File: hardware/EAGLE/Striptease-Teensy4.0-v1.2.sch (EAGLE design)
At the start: 18 parts, among them IC1 74245N

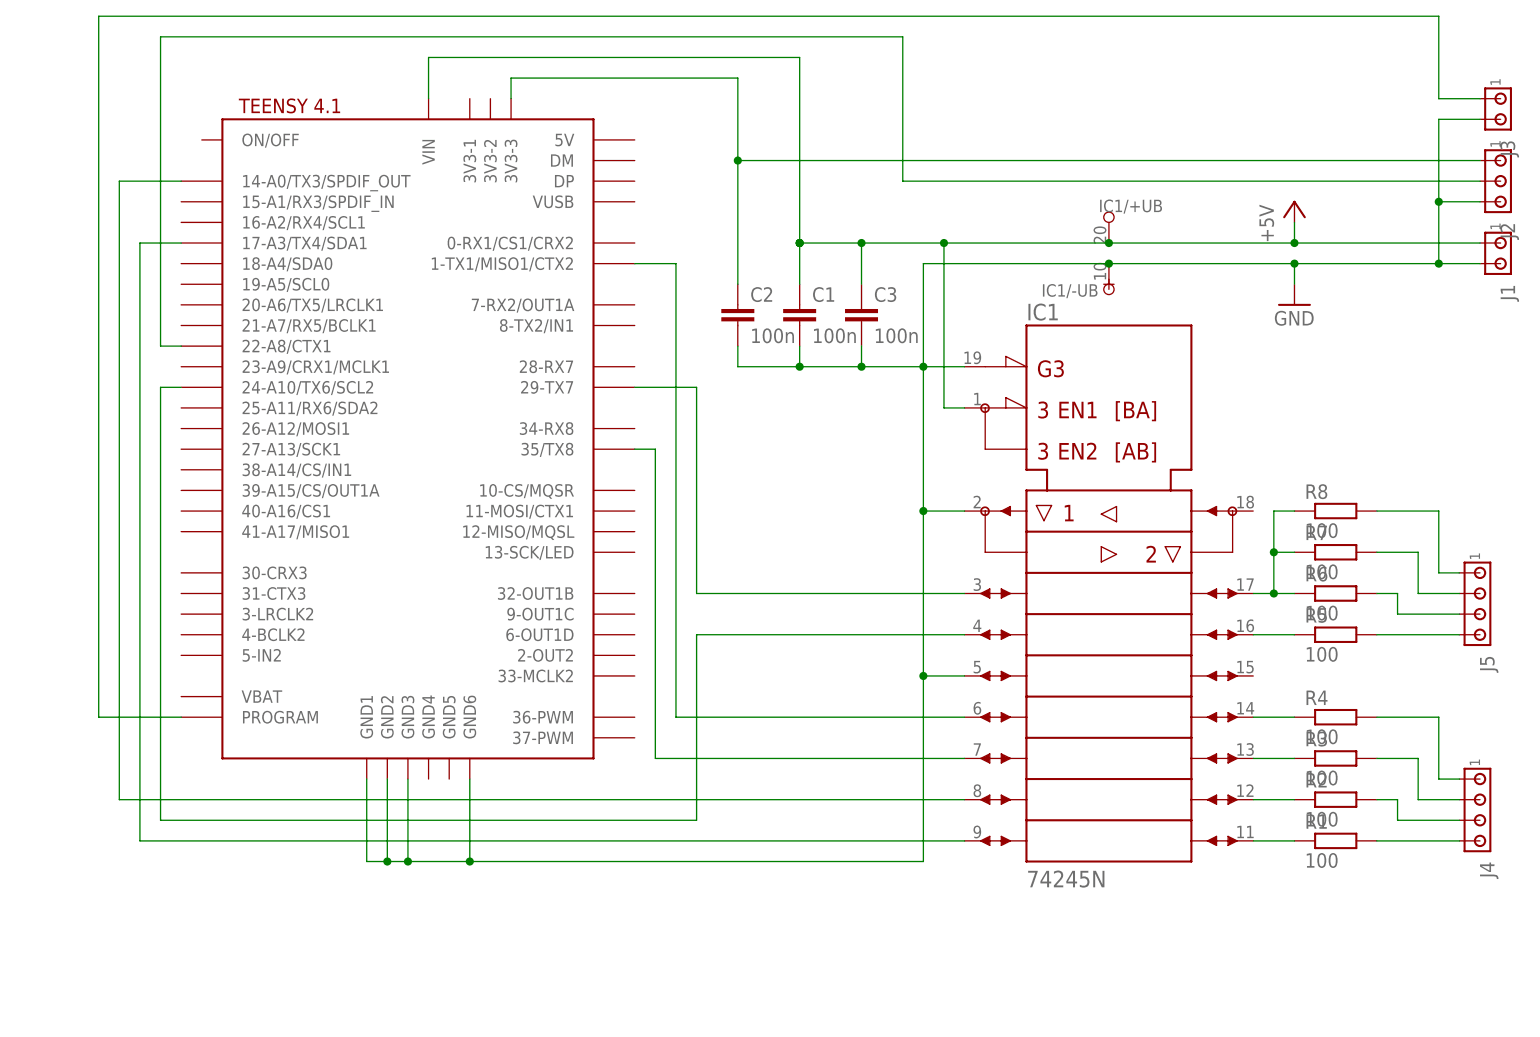
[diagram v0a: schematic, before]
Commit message: Change connector names in EAGLE boards.
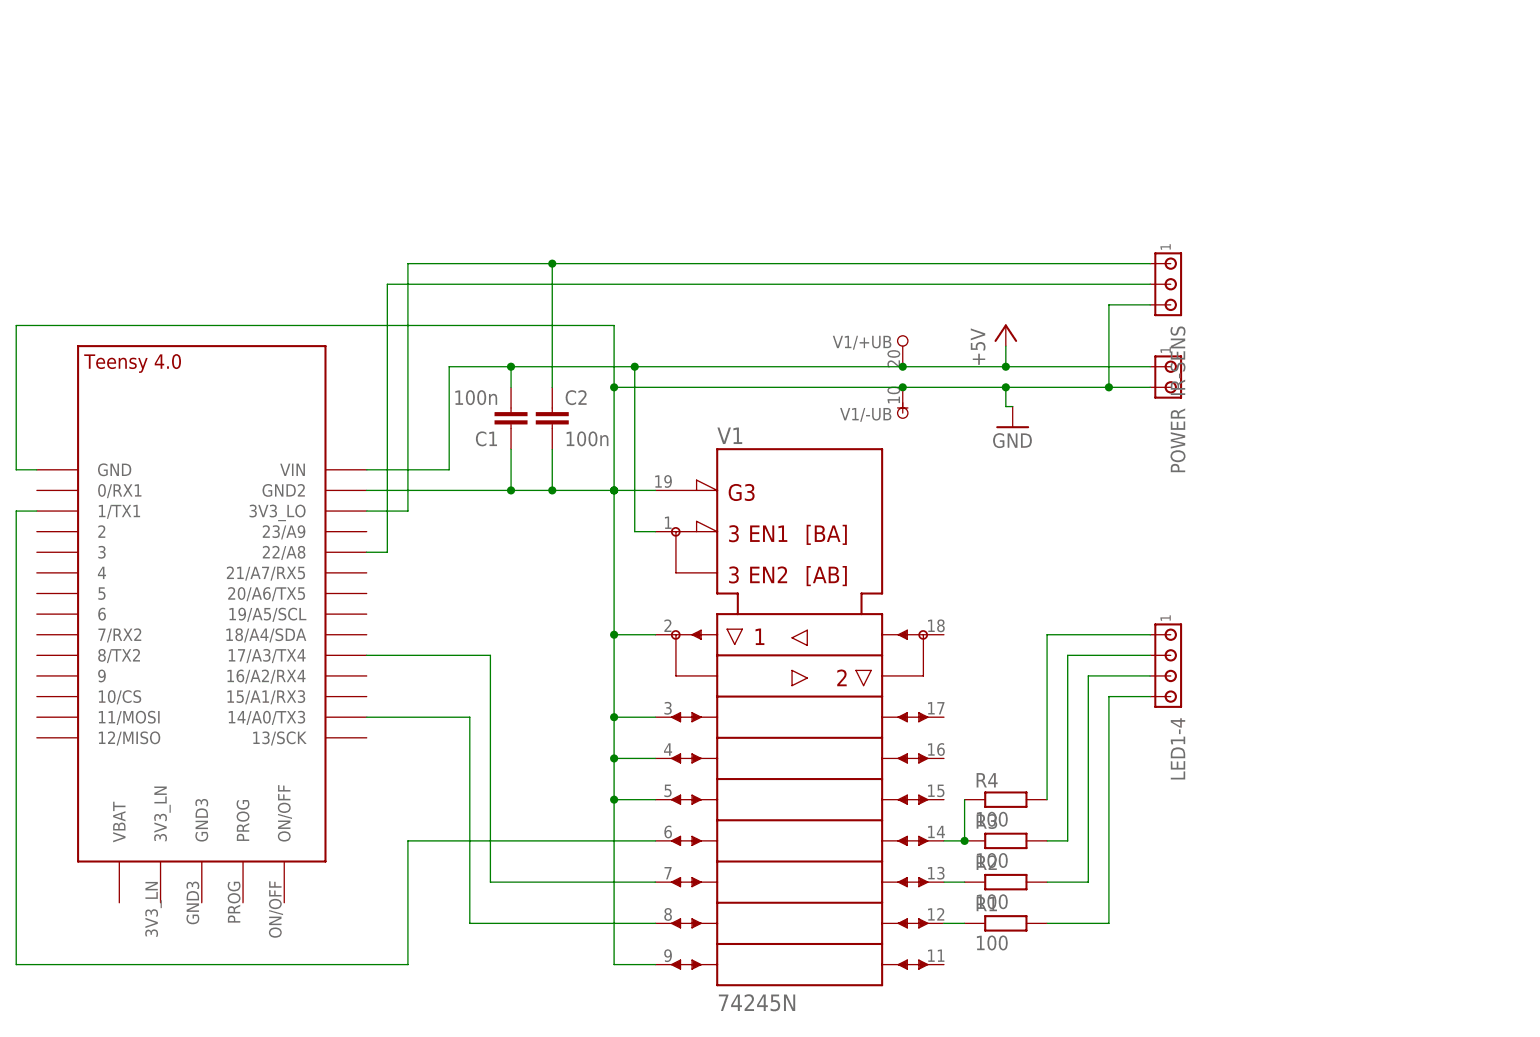
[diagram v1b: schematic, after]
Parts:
- removed C3: 100n, rcl:C-EU050-025X075
- removed IC1: 74245N, 74ttl-din:74245N
- removed J1, J3: (no value), con-amp:MTA02-100
- removed J2: (no value), con-amp:MTA03-100
- removed J4, J5: (no value), con-amp:MTA04-100
- removed R5, R6, R7, R8: 100, rcl:R-EU_0207/10
- removed U$3: TEENSY41-E, teensy:TEENSY41-E
- added IR-SENS: (no value), con-amp:MTA03-100
- added LED1-4: (no value), con-amp:MTA04-100
- added POWER: (no value), con-amp:MTA02-100
- added U$1: TEENSY_4.0-BASIC, Teensy-4.0:TEENSY_4.0-BASIC
- added V1: 74245N, 74ttl-din:74245N
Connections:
- removed net N$16: IC11.B5, R4.1
- removed net N$19: J4.1, R4.2
- removed net N$20: J5.4, R5.2
- removed net N$22: J5.3, R6.2
- removed net N$23: IC11.A8, U$3.17-A3/TX4/SDA1
- removed net N$24: IC11.A7, U$3.14-A0/TX3/SPDIF_OUT
- removed net N$25: IC11.A6, U$3.35/TX8
- removed net N$26: IC11.A5, U$3.1-TX1/MISO1/CTX2
- removed net N$27: IC11.A3, U$3.24-A10/TX6/SCL2
- removed net N$28: IC11.A2, U$3.29-TX7
- removed net N$3: IC11.B3, R5.1
- removed net N$31: J2.2, U$3.22-A8/CTX1
- removed net N$6: J5.2, R7.2
- new net N$21: U$1.1/TX1, V11.A5
- new net N$5: LED1-4.1, R4.2
- net +5V: now also C1.2, POWER.1, U$1.VIN, V1/+UB.+UB, V11.DIR; no longer C1.1, C3.1, IC1/+UB.+UB, IC11.DIR, J1.1, U$3.VIN
- net GND: now also C1.1, IR-SENS.3, POWER.2, U$1.GND, U$1.GND2, V1/-UB.-UB, V11.!G, V11.A1, V11.A2, V11.A3, V11.A4, V11.A8; no longer C1.2, C3.2, IC1/-UB.-UB, IC11.!G, IC11.A1, IC11.A4, J1.2, J2.3, J3.2, U$3.GND1, U$3.GND2, U$3.GND3, U$3.GND6
- net N$1: now also IR-SENS.2, U$1.22/A8; no longer C2.1, J2.1, U$3.3V3-3
- net N$10: now also U$1.14/A0/TX3, V11.A7; no longer J5.1, R8.2
- net N$11: now also V11.B7; no longer IC11.B8
- net N$12: now also V11.B6; no longer IC11.B7
- net N$13: now also R4.1, V11.B5; no longer IC11.B6
- net N$14: now also U$1.17/A3/TX4, V11.A6; no longer IC11.B2, R6.1, R7.1, R8.1
- net N$2: now also C2.1, IR-SENS.1, U$1.3V3_LO; no longer J3.1, U$3.PROGRAM
- net N$7: now also LED1-4.2; no longer J4.2
- net N$8: now also LED1-4.3; no longer J4.3
- net N$9: now also LED1-4.4; no longer J4.4
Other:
- moved on the sheet: C1, C2, R1, R2, R3, R4

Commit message: Add connector pinout for LEDs in EAGLE boards.
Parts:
- renumbered IR-SENS to IR-RECV
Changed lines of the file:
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@@
 <part name="R3" library="rcl" library_urn="urn:adsk.eagle:library:334" deviceset="R-EU_" device="0207/10" package3d_urn="urn:adsk.eagle:package:23491/2" value="100"/>
 <part name="LED1-4" library="con-amp" library_urn="urn:adsk.eagle:library:127" deviceset="MTA04-100" device="" package3d_urn="urn:adsk.eagle:package:8081620/1"/>
-<part name="IR-SENS" library="con-amp" library_urn="urn:adsk.eagle:library:127" deviceset="MTA03-100" device="" package3d_urn="urn:adsk.eagle:package:8081621/1"/>
+<part name="IR-RECV" library="con-amp" library_urn="urn:adsk.eagle:library:127" deviceset="MTA03-100" device="" package3d_urn="urn:adsk.eagle:package:8081621/1"/>
 <part name="POWER" library="con-amp" library_urn="urn:adsk.eagle:library:127" deviceset="MTA02-100" device="" package3d_urn="urn:adsk.eagle:package:8081649/1"/>
 <part name="P+1" library="supply1" library_urn="urn:adsk.eagle:library:371" deviceset="+5V" device=""/>
@@
 <attribute name="VALUE" x="143.51" y="35.56" size="1.778" layer="96" rot="R270"/>
 </instance>
-<instance part="IR-SENS" gate="G$1" x="147.32" y="88.9" smashed="yes" rot="R270">
+<instance part="IR-RECV" gate="G$1" x="147.32" y="88.9" smashed="yes" rot="R270">
 <attribute name="NAME" x="147.32" y="83.82" size="1.778" layer="95" rot="R270"/>
 <attribute name="VALUE" x="143.51" y="83.82" size="1.778" layer="96" rot="R270"/>
@@
 <pinref part="U$1" gate="G$1" pin="22/A8"/>
 <wire x1="50.8" y1="55.88" x2="48.26" y2="55.88" width="0.1524" layer="91"/>
-<pinref part="IR-SENS" gate="G$1" pin="2"/>
+<pinref part="IR-RECV" gate="G$1" pin="2"/>
 <wire x1="50.8" y1="88.9" x2="144.78" y2="88.9" width="0.1524" layer="91"/>
 </segment>
@@
 <wire x1="71.12" y1="91.44" x2="53.34" y2="91.44" width="0.1524" layer="91"/>
 <junction x="71.12" y="91.44"/>
-<pinref part="IR-SENS" gate="G$1" pin="1"/>
+<pinref part="IR-RECV" gate="G$1" pin="1"/>
 <wire x1="71.12" y1="91.44" x2="144.78" y2="91.44" width="0.1524" layer="91"/>
 </segment>
@@
 <net name="GND" class="0">
 <segment>
-<pinref part="IR-SENS" gate="G$1" pin="3"/>
+<pinref part="IR-RECV" gate="G$1" pin="3"/>
 <wire x1="139.7" y1="86.36" x2="144.78" y2="86.36" width="0.1524" layer="91"/>
 <pinref part="POWER" gate="G$1" pin="2"/>
